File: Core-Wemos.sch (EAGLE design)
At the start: 23 parts, among them IC1 7805, J3 CONNECTOR-GROVE-4P-2.0-347013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

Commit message: 2.0
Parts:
- removed C6: 150uF, SPCoast:CAP-POL0810
- removed IC1: 7805, SPCoast:VREG_78XX-1300040P1
- removed J4: (no value), SPCoast:CONNECTOR-DC-POWER-RA
- removed J5: (no value), SPCoast:CONNECTOR-RJ25CORCOM
- removed JP10, JP11: (no value), SparkFun-Connectors:M06LOCK
- removed JP5: 5v I2C Power, SparkFun-Connectors:M02LOCK
- removed R101, R111: 1k8, SPCoast:RPTH-1/6W
- removed U$2: (no value), SPCoast:WEMOS-D1V1
- removed U$3: 9-12vDC, SPCoast-minimal:POWER_LABEL
- removed U$4: BOARD80X100, SPCoast:BOARD80X100
- removed U$5, U$6: VMATCH, SPCoast:VMATCH
- added BOARD: BOARD80X150, SPCoast:BOARD80X150
- added CON3: (no value), SPCoast:JUMPER-3PTH-LOCK
- added J1: (no value), SPCoast:CONNECTOR-DC-POWER-RA
- added JP2: 5v I2C Power, SparkFun-Connectors:M02LOCK
- added JP3: (no value), SparkFun-Connectors:M06LOCK
- added LABEL1: 7-12vDC, SPCoast-minimal:POWER_LABEL
- added LED1, LED2: LEDMATRIX, SPCoast:LEDMATRIX
- added LS1, LS2, LS3: (no value), SPCoast:I2C-LEVELSHIFTER
- added VR5.0: 5v, SPCoast:VREG-DPAK-5
- added WEMOS: D1Mini, SPCoast:WEMOS-D1V1
- C1, C2: value 1uF -> 150uF; device SPCoast:CAP0805 -> SPCoast:CAP-POL0810
- C3, C4: value 1uF -> 0.1uF
- C5: value 150uF -> 0.1uF; device SPCoast:CAP-POL0810 -> SPCoast:CAP0805
- J2: value (none) -> CONNECTOR-GROVE-4P-2.0-3470130P1; device SPCoast:CONNECTOR-RJ25CORCOM -> SPCoast:CONNECTOR-GROVE-4P-2.0-3470130P1
- J3: value CONNECTOR-GROVE-4P-2.0-3470130P1 -> (none); device SPCoast:CONNECTOR-GROVE-4P-2.0-3470130P1 -> SPCoast:CONNECTOR-RJ25TOP
- renumbered U$1 to OSHW1
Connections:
- removed net +3V3: U$2.3V3, U$5.VL, U$6.VL
- removed net A0: U$2.A0
- removed net D8: U$2.D8
- new net 3V3: LS1.VL, LS2.VL, LS3.VL, WEMOS.3V3
- new net N$10: LED1.CLK@2, LED2.CLK@1
- new net N$3: LED1.DOUT, LED2.DIN
- new net N$9: LED1.CS@2, LED2.CS@1
- new net RXH: J3.4, JP3.4, LS1.H2
- new net TXH: J3.5, JP3.5, LS1.H1
- net +9V: now also C1.+, C2.+, C4.1, J1.1, J2.3, J2.4, VR5.0.IN; no longer C2.1, C5.+, IC1.IN, J3.3, J3.4, J4.1
- net D0: now also LS1.L4, WEMOS.D0; no longer U$2.D0, U$6.L1
- net D0H: now also J3.2, JP3.2, LS1.H4; no longer J2.2, JP10.2, U$6.H1
- net D3: now also LS2.L4, WEMOS.D3; no longer U$2.D3, U$6.L4
- net D3H: now also CON3.2, LS2.H4; no longer J2.3, JP10.3, U$6.H4
- net D4: now also LS2.L3, WEMOS.D4; no longer U$2.D4, U$5.L1
- net D4H: now also LED1.DIN, LS2.H3; no longer J2.4, JP10.4, U$5.H1
- net D5: now also LS2.L2, WEMOS.D5; no longer U$2.D5, U$5.L2
- net D5H: now also LED1.CS@1, LS2.H2; no longer J2.5, JP10.5, U$5.H2
- net D6: now also LS2.L1, WEMOS.D6; no longer U$2.D6, U$5.L4
- net D6H: now also LED1.CLK@1, LS2.H1; no longer J5.2, JP11.2, U$5.H4
- net D7: now also LS1.L3, WEMOS.D7; no longer U$2.D7, U$5.L3
- net D7H: now also J3.3, JP3.3, LS1.H3; no longer J5.3, JP11.3, U$5.H3
- net GND: now also C1.-, C2.-, C5.2, CON3.3, J1.2, J1.3, J2.1, J2.2, J3.6, JP3.6, LED1.G@1, LED1.G@2, LED2.G@1, LED2.G@2, LS1.GND@0, LS1.GND@1, LS2.GND@0, LS2.GND@1, LS3.GND@0, LS3.GND@1, VR5.0.GND, WEMOS.GND; no longer C1.2, C2.2, C5.-, C6.-, IC1.GND, J2.6, J3.1, J3.2, J4.2, J4.3, J5.6, JP10.6, JP11.6, U$2.GND, U$5.GND@0, U$5.GND@1, U$6.GND@0, U$6.GND@1
- net N$44: now also JP2.1; no longer JP5.1
- net RX: now also LS1.L2, WEMOS.RX; no longer J5.4, JP11.4, U$2.RX
- net SCL: now also LS3.L2, WEMOS.D1; no longer U$2.D1, U$6.L2
- net SCLH: now also LS3.H2; no longer R111.2, U$6.H2
- net SDA: now also LS3.L1, WEMOS.D2; no longer U$2.D2, U$6.L3
- net SDAH: now also LS3.H1; no longer R101.2, U$6.H3
- net TX: now also LS1.L1, WEMOS.TX; no longer J5.5, JP11.5, U$2.TX
- net VCCIO: now also C5.1, CON3.1, J3.1, JP2.2, JP3.1, LED1.V+@1, LED1.V+@2, LED2.V+@1, LED2.V+@2, LS1.VH, LS2.VH, LS3.VH, VR5.0.OUT, WEMOS.5V; no longer C1.1, C4.1, C6.+, IC1.OUT, J2.1, J5.1, JP10.1, JP11.1, JP5.2, R101.1, R111.1, U$2.5V, U$5.VH, U$6.VH
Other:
- note added: "2.0"
- note added: "3v / 5v I/O level shifting"
- note added: "CS"
- note added: "Codeline Matrix"
- note added: "DATA"
- note added: "I2C"
- note added: "IO & I2C Adapter for WeMOS D1"
- note added: "IO1"
- note added: "IO4"
- note added: "MC"
- note added: "Processor carrier board for WeMOS D1 Breaks out 5v I2C, IO4 style header for direct IO, Maintainer Call and Matrix Display"
- note added: "WeMos D1 Mini R2"
- note added: "clock"
- note removed: "1.0"
- note removed: "16 bit Arduino I2C I/O card"
- note removed: "IO4-Adapter for WeMOS D1"
- note removed: "Note: New WeMOS/ESP8266 processor - based on Photon 2.0"
- moved on the sheet: C3, C4, I2C

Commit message: 3.0
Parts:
- removed LS1, LS2, LS3: (no value), SPCoast:I2C-LEVELSHIFTER
- added Q1, Q10, Q2, Q3, Q4, Q5, Q6, Q7, Q8, Q9: (no value), SPCoast:MOSFET-N-BSS138-SOT23
- added R1, R10, R11, R12, R13, R14, R15, R16, R17, R18, R19, R2, R20, R3, R4, R5, R6, R7, R8, R9: 10k, SPCoast:R0805-RES
- C3: value 0.1uF -> 10uF
- C4: value 0.1uF -> 1.0uF
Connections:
- removed net 3V3: LS1.VL, LS2.VL, LS3.VL, WEMOS.3V3
- new net +3V3: Q1.G, Q10.G, Q2.G, Q3.G, Q4.G, Q5.G, Q6.G, Q7.G, Q8.G, Q9.G, R1.2, R11.2, R13.2, R15.2, R17.2, R19.2, R2.2, R5.2, R7.2, R9.2, WEMOS.3V3
- net D0: now also Q7.S, R13.1; no longer LS1.L4
- net D0H: now also Q7.D, R14.1; no longer LS1.H4
- net D3: now also Q1.S, R1.1; no longer LS2.L4
- net D3H: now also Q1.D, R4.1; no longer LS2.H4
- net D4: now also Q10.S, R19.1; no longer LS2.L3
- net D4H: now also Q10.D, R20.1; no longer LS2.H3
- net D5: now also Q9.S, R17.1; no longer LS2.L2
- net D5H: now also Q9.D, R18.1; no longer LS2.H2
- net D6: now also Q8.S, R15.1; no longer LS2.L1
- net D6H: now also Q8.D, R16.1; no longer LS2.H1
- net D7: now also Q6.S, R11.1; no longer LS1.L3
- net D7H: now also Q6.D, R12.1; no longer LS1.H3
- net GND: no longer LS1.GND@0, LS1.GND@1, LS2.GND@0, LS2.GND@1, LS3.GND@0, LS3.GND@1
- net RX: now also Q5.S, R9.1; no longer LS1.L2
- net RXH: now also Q5.D, R10.1; no longer LS1.H2
- net SCL: now also Q3.S, R5.1; no longer LS3.L2
- net SCLH: now also Q3.D, R6.1; no longer LS3.H2
- net SDA: now also Q2.S, R2.1; no longer LS3.L1
- net SDAH: now also Q2.D, R3.1; no longer LS3.H1
- net TX: now also Q4.S, R7.1; no longer LS1.L1
- net TXH: now also Q4.D, R8.1; no longer LS1.H1
- net VCCIO: now also R10.2, R12.2, R14.2, R16.2, R18.2, R20.2, R3.2, R4.2, R6.2, R8.2; no longer LS1.VH, LS2.VH, LS3.VH
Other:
- moved on the sheet: C5, CON3, I2C, J3, JP2, JP3, LED1, LED2, WEMOS

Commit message: removed Matrix display, added OLED, shrunk
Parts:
- removed C5: 0.1uF, SPCoast:CAP0805
- removed CON3: (no value), SPCoast:JUMPER-3PTH-LOCK
- removed JP3: (no value), SparkFun-Connectors:M06LOCK
- removed LED1, LED2: LEDMATRIX, SPCoast:LEDMATRIX
- removed Q10: (no value), SPCoast:MOSFET-N-BSS138-SOT23
- removed R19, R20: 10k, SPCoast:R0805-RES
- added CON1: (no value), SPCoast:CONNECTOR-M05CMRI
- added CON2: (no value), SPCoast:CONNECTOR-I2CNOOUTLINE
- added FID1, FID2, FID3, FID4: FIDUCIAL, SPCoast:FIDUCIAL
- added JP1: 5v I2C Power, SparkFun-Connectors:M02LOCK
- BOARD: device SPCoast:BOARD80X150 -> SPCoast:BOARD80X80
- C1: value 150uF -> 1.0uF; device SPCoast:CAP-POL0810 -> SPCoast:CAP0805
- C2: value 150uF -> 10uF; device SPCoast:CAP-POL0810 -> SPCoast:CAP0805
- C3: value 10uF -> 150uF; device SPCoast:CAP0805 -> SPCoast:CAP-POL0810
- C4: value 1.0uF -> 0.1uF
- J3: device SPCoast:CONNECTOR-RJ25TOP -> SPCoast:CONNECTOR-RJ25-6P6C
- JP2: value 5v I2C Power -> (none); device SparkFun-Connectors:M02LOCK -> SparkFun-Connectors:M06LOCK
- LABEL1: device SPCoast-minimal:POWER_LABEL -> SPCoast:DOC-POWER_LABEL
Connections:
- removed net D0: Q7.S, R13.1, WEMOS.D0
- removed net D0H: J3.2, JP3.2, Q7.D, R14.1
- removed net N$10: LED1.CLK@2, LED2.CLK@1
- removed net N$3: LED1.DOUT, LED2.DIN
- removed net N$9: LED1.CS@2, LED2.CS@1
- net +3V3: now also CON2.V+, R3.2, R4.2, R6.2, R8.2; no longer Q10.G, R11.2, R13.2, R15.2, R17.2, R19.2
- net +9V: now also C1.1, C3.+; no longer C1.+, C2.+, C4.1
- net D3: now also Q7.S, R7.1; no longer Q1.S, R1.1
- net D3H: now also J3.2, JP2.2, Q7.D, R16.1; no longer CON3.2, Q1.D, R4.1
- net D4: now also Q6.S, R6.1; no longer Q10.S, R19.1
- net D4H: now also J3.3, JP2.3, Q6.D, R15.1; no longer LED1.DIN, Q10.D, R20.1
- net D5: now also Q5.S, R5.1; no longer Q9.S, R17.1
- net D5H: now also J3.4, JP2.4, Q5.D, R14.1; no longer LED1.CS@1, Q9.D, R18.1
- net D6: now also Q4.S, R4.1; no longer Q8.S, R15.1
- net D6H: now also J3.5, JP2.5, Q4.D, R13.1; no longer LED1.CLK@1, Q8.D, R16.1
- net D7: now also Q3.S, R3.1; no longer Q6.S, R11.1
- net D7H: now also CON1.5, Q3.D; no longer J3.3, JP3.3, Q6.D
- net GND: now also C1.2, C2.2, C3.-, CON1.1, CON2.GND, JP2.6; no longer C1.-, C2.-, C3.2, C5.2, CON3.3, JP3.6, LED1.G@1, LED1.G@2, LED2.G@1, LED2.G@2
- net N$44: now also JP1.1; no longer JP2.1
- net RX: now also Q2.S, R2.1; no longer Q5.S, R9.1
- net RXH: now also CON1.4, Q2.D, R11.1; no longer J3.4, JP3.4, Q5.D, R10.1
- net SCL: now also CON2.SCL, Q9.S, R9.1; no longer Q3.S, R5.1
- net SCLH: now also Q9.D, R18.1; no longer Q3.D, R6.1
- net SDA: now also CON2.SDA, Q8.S, R8.1; no longer Q2.S, R2.1
- net SDAH: now also Q8.D, R17.1; no longer Q2.D, R3.1
- net TX: now also Q1.S, R1.1; no longer Q4.S, R7.1
- net TXH: now also CON1.3, Q1.D, R10.1; no longer J3.5, JP3.5, Q4.D, R8.1
- net VCCIO: now also C2.1, C4.1, CON1.2, JP1.2, JP2.1, R11.2, R13.2, R15.2, R17.2; no longer C3.1, C5.1, CON3.1, JP2.2, JP3.1, LED1.V+@1, LED1.V+@2, LED2.V+@1, LED2.V+@2, R20.2, R3.2, R4.2, R6.2, R8.2
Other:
- note added: "3v3"
- note added: "5V"
- note removed: "CS"
- note removed: "Codeline Matrix"
- note removed: "DATA"
- note removed: "IO1"
- note removed: "MC"
- note removed: "clock"
- moved on the sheet: C4, Q1, Q2, Q3, Q4, Q5, Q6, Q7, Q8, Q9, R1, R10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

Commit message: realigned I2C connectors, added power on LED
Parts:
- added LED18: G, SPCoast:LED0603-LED
- added R19: 2K0, SPCoast:R0603-RES
- BOARD: device SPCoast:BOARD80X80 -> SPCoast:BOARD80X80-NOHOLES
- J3: value (none) -> IO4
- renumbered CON1 to CMRI-IO, CON2 to I2C-OLED
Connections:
- new net GND1: R19.2
- new net N$1: LED18.C, R19.1
- net VCCIO: now also LED18.A

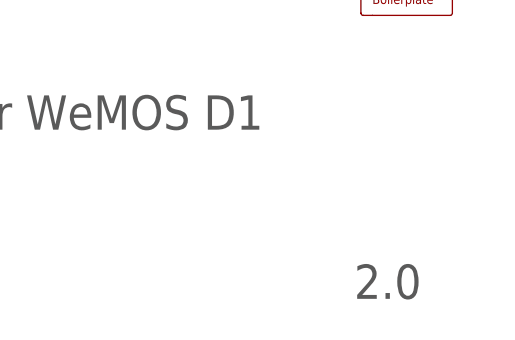
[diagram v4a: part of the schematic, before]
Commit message: Silkscreen 4.0 change
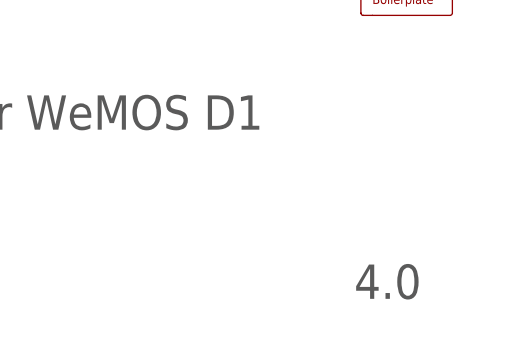
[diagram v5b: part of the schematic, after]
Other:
- note added: "4.0"
- note removed: "2.0"
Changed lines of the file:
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@@
 <text x="149.86" y="25.4" size="3.81" layer="97">IO &amp; I2C Adapter for WeMOS D1</text>
 <text x="152.908" y="6.35" size="3.81" layer="97">John Plocher</text>
-<text x="235.458" y="6.604" size="3.81" layer="97">2.0</text>
+<text x="235.458" y="6.604" size="3.81" layer="97">4.0</text>
 <text x="149.86" y="38.1" size="1.6764" layer="102">Processor carrier board for WeMOS D1
 Breaks out 5v I2C, IO4 style header for direct IO,
